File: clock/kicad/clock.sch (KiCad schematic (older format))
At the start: 82 parts, among them J1 USB-SS-52100-001, Q1 PN2222A, SW1 HOUR, SW2 MIN, SW3 TIME, U1 74HC4060, U10 74HC390, U11 NE555P, U12 74HC4511, U13 74HC4511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

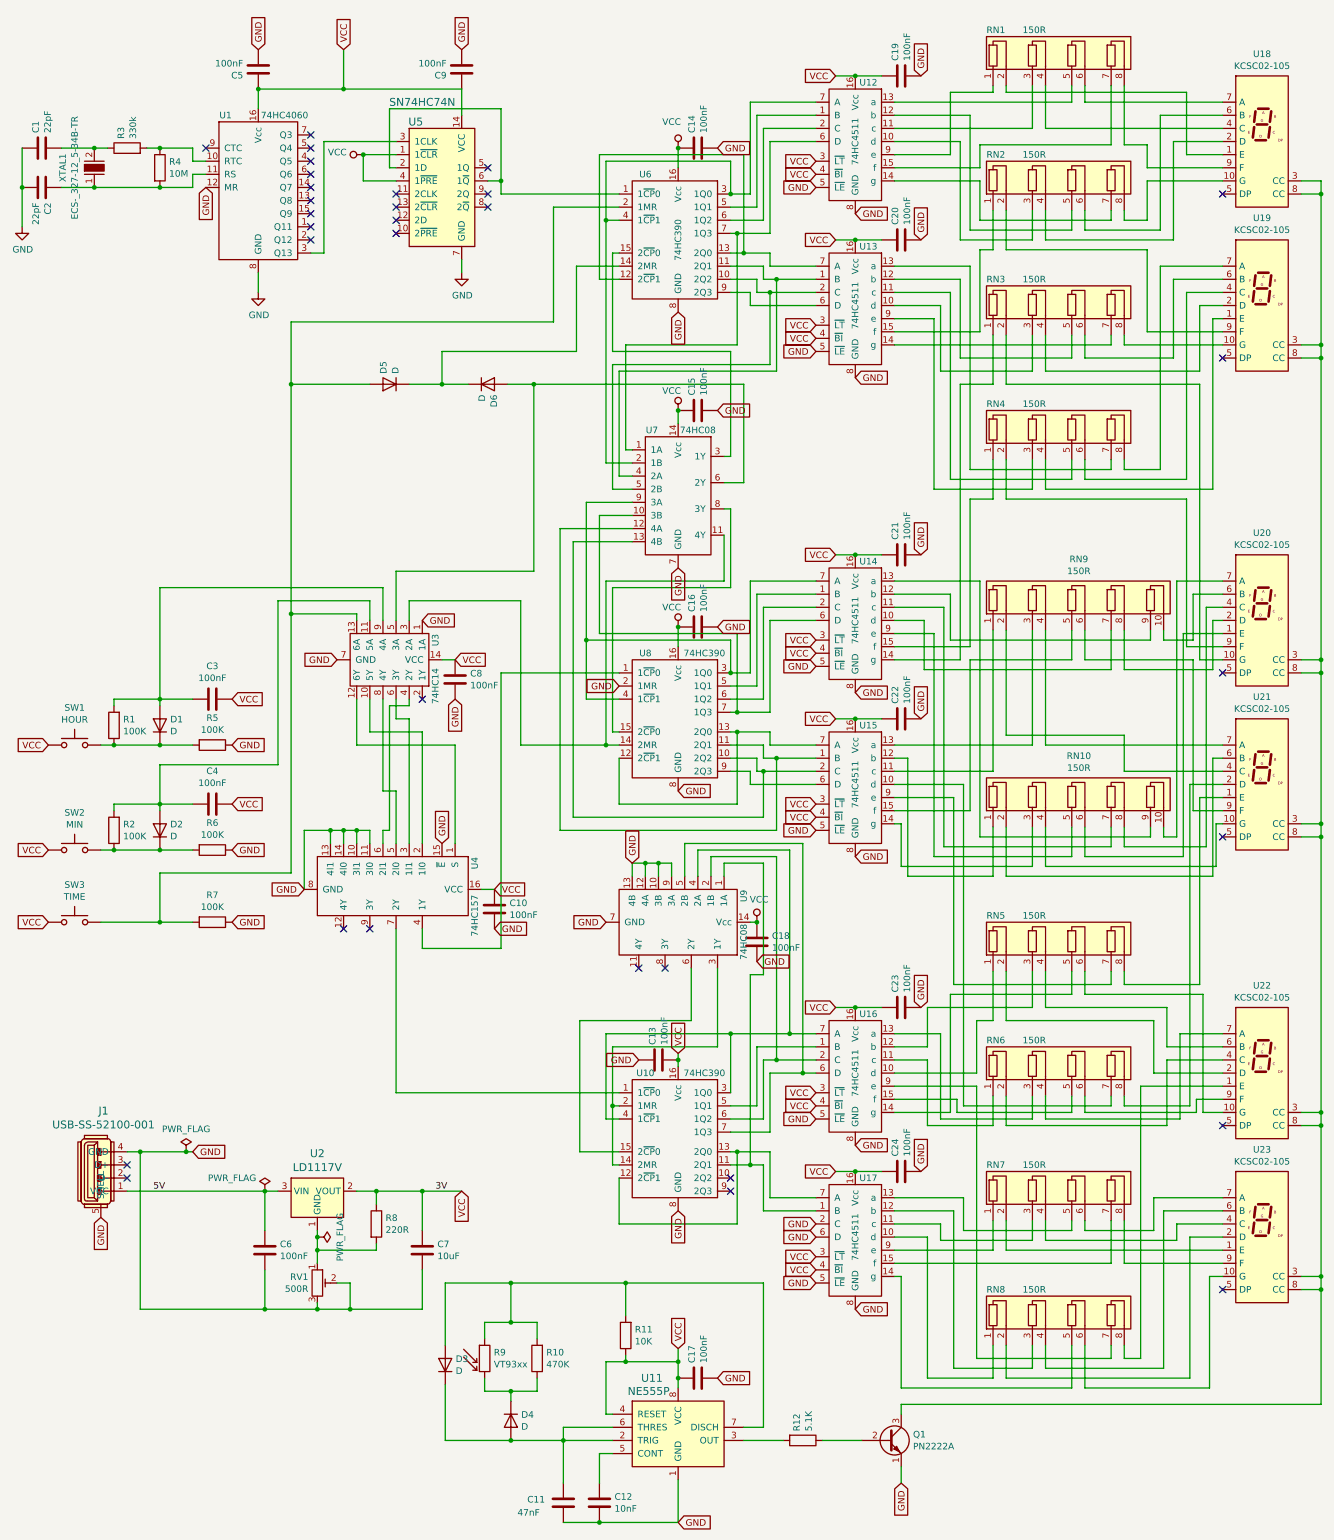
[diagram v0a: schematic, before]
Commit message: Clock: Switched 24H counter's high digit to quinary counter to match breadboard version.
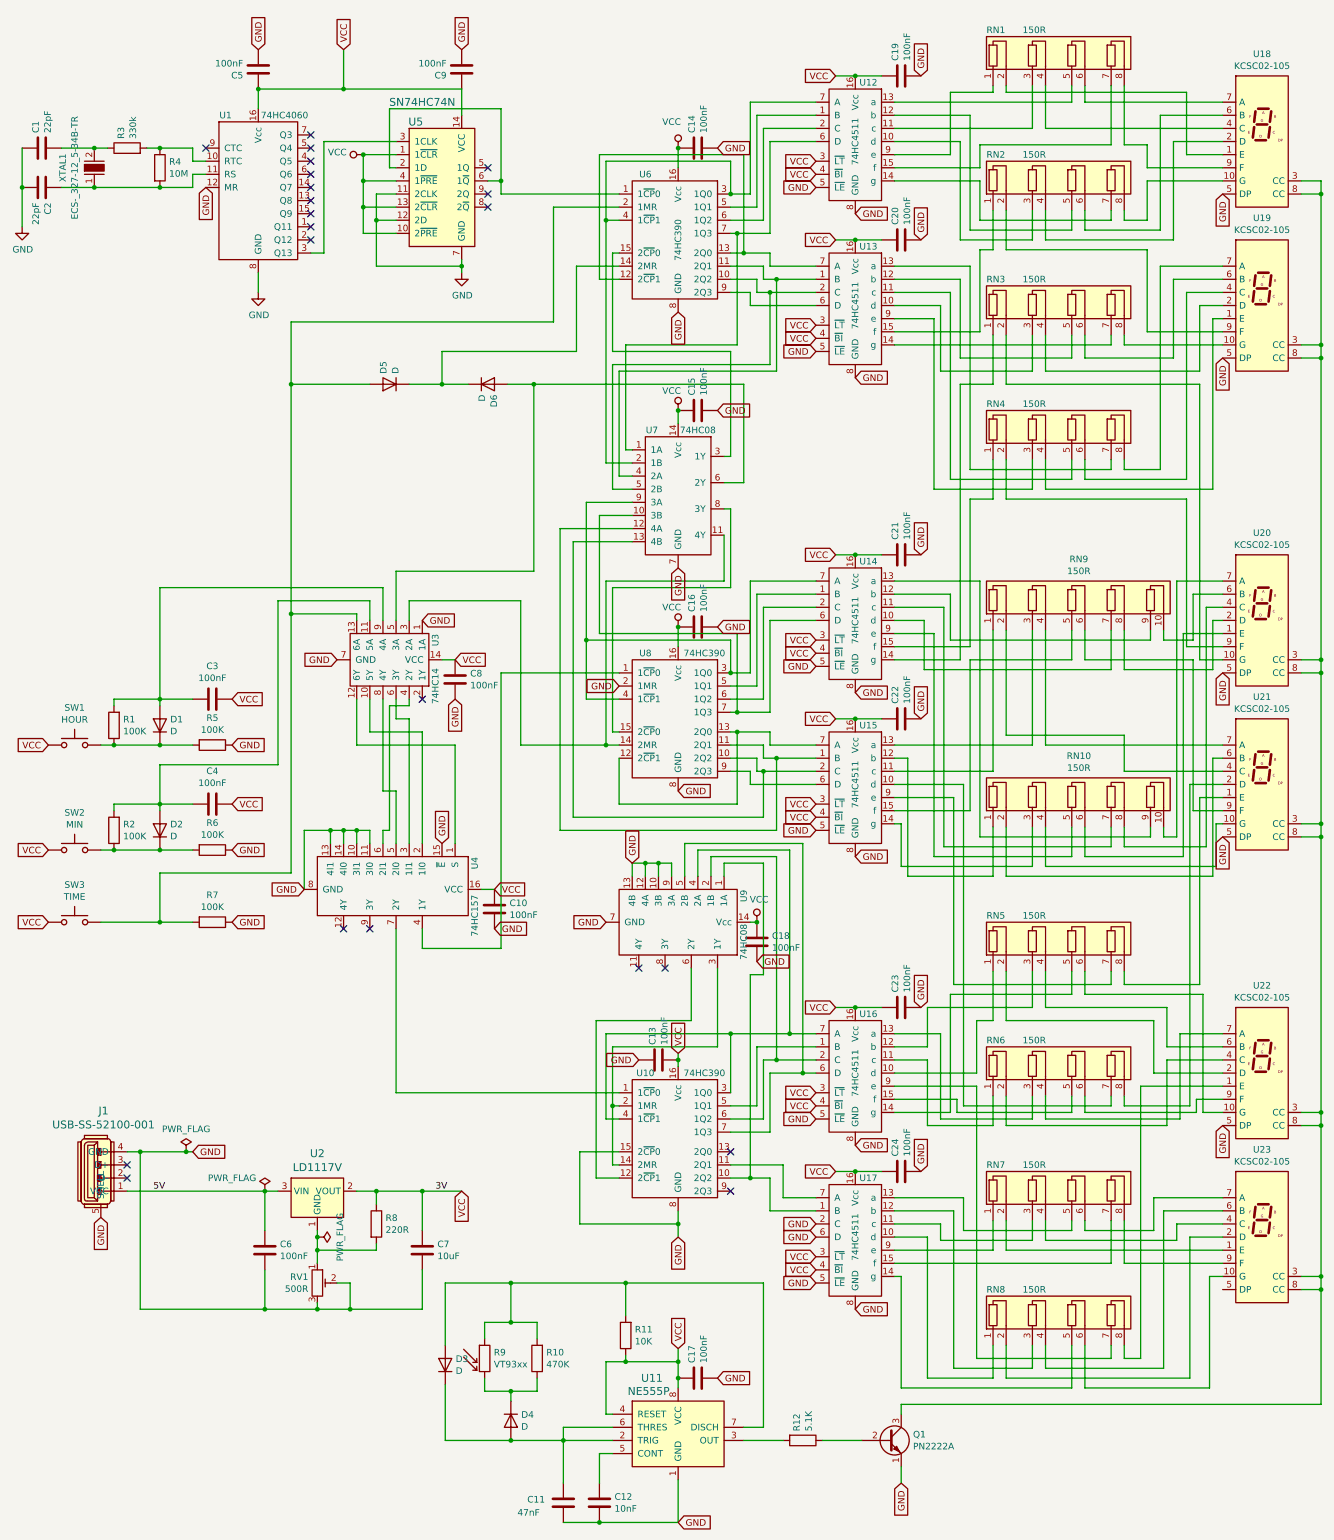
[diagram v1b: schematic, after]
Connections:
- net GND: now also U10.15 (2~CP~0), U18.5 (DP), U19.5 (DP), U20.5 (DP), U21.5 (DP), U22.5 (DP), U5.11 (2CLK), U5.12 (2D)
- net VCC: now also U5.10 (2~PRE), U5.13 (2~CLR)
- net at U17.1 (B), U9.1 (1A): now also U10.10 (2Q2); no longer U10.11 (2Q1)
- net at U9.6 (2Y): now also U10.12 (2~CP~1); no longer U10.15 (2~CP~0)
- new net: U10.11 (2Q1), U17.7 (A)
- now unconnected: U10.13 (2Q0)
- no-connect marks 32 -> 22
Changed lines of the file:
@@
 	2550 2450 2550 2600
 Wire Wire Line
-	4100 2350 4100 2450
+	4100 2350 4100 2400
 Wire Wire Line
 	3600 1650 3550 1650
@@
 	1    0    0    -1
 $EndComp
-NoConn ~ 3600 1850
-NoConn ~ 3600 1950
-NoConn ~ 3600 2050
-NoConn ~ 3600 2150
 NoConn ~ 2950 2200
 NoConn ~ 2950 2100
@@
 	1    0    0    -1
 $EndComp
-NoConn ~ 9900 1850
-NoConn ~ 9900 3100
 $Comp
 L clock:74HC390 U8
@@
 	1    0    0    -1
 $EndComp
-NoConn ~ 9900 5500
 Wire Wire Line
 	5150 5200 5150 4300
@@
 Wire Wire Line
 	6450 9000 6150 9000
-Wire Wire Line
-	6450 9150 6200 9150
-Wire Wire Line
-	6400 9250 6300 9250
-Text GLabel 5750 9600 3    50   Input ~ 0
+Text GLabel 5750 9800 3    50   Input ~ 0
 GND
 Text GLabel 5750 8400 1    50   Input ~ 0
@@
 	6700 6800 5800 6800
 Wire Wire Line
-	5800 6800 5800 7050
-Wire Wire Line
 	6350 8350 6800 8350
 Wire Wire Line
@@
 	5850 7750 5850 8150
 Wire Wire Line
-	5850 8150 5000 8150
-Wire Wire Line
-	5000 8150 5000 9150
-Wire Wire Line
-	5000 9150 5300 9150
-Wire Wire Line
-	6200 9150 6200 9700
-Wire Wire Line
-	6200 9700 5300 9700
-Wire Wire Line
-	5300 9700 5300 9350
-Connection ~ 6200 9150
-Wire Wire Line
-	6200 9150 6150 9150
-NoConn ~ 6150 9350
+	5850 8150 5125 8150
 NoConn ~ 6150 9450
 Text GLabel 6800 6600 0    50   Input ~ 0
@@
 Text GLabel 6800 6700 0    50   Input ~ 0
 GND
-NoConn ~ 9900 6750
 Text GLabel 7100 6900 2    50   Input ~ 0
 GND
@@
 	6150 8250 6600 8250
 Wire Wire Line
-	6300 9250 6300 7800
-Wire Wire Line
 	6300 7800 6400 7800
 Wire Wire Line
@@
 Wire Wire Line
 	6100 6950 6100 7050
-Connection ~ 6300 9250
-Wire Wire Line
-	6300 9250 6150 9250
 Text GLabel 2150 1800 3    50   Input ~ 0
 GND
@@
 Wire Wire Line
 	7450 11075 7450 11150
-Wire Wire Line
-	6400 9600 6400 9250
-Wire Wire Line
-	6450 9500 6450 9150
 Text GLabel 7600 9300 1    50   Input ~ 0
 GND
@@
 	1    0    0    -1
 $EndComp
-Wire Wire Line
-	6400 9600 6800 9600
-Wire Wire Line
-	6450 9500 6800 9500
-NoConn ~ 9900 10200
-NoConn ~ 9900 8950
 Connection ~ 10650 10200
 Connection ~ 10650 10100
@@
 	9150 2050 9325 2050
 Wire Wire Line
-	9325 2050 9325 1750
-Wire Wire Line
-	9325 1750 9900 1750
-Wire Wire Line
 	7400 2900 8050 2900
 Wire Wire Line
@@
 Wire Wire Line
 	2800 3300 2800 5050
+Wire Wire Line
+	3350 1750 3350 1950
+Wire Wire Line
+	3350 2150 3600 2150
+Connection ~ 3350 1750
+Wire Wire Line
+	3600 1950 3350 1950
+Connection ~ 3350 1950
+Wire Wire Line
+	3350 1950 3350 2150
+Wire Wire Line
+	3600 1850 3450 1850
+Wire Wire Line
+	3450 1850 3450 2050
+Wire Wire Line
+	3450 2400 4100 2400
+Connection ~ 4100 2400
+Wire Wire Line
+	4100 2400 4100 2450
+Wire Wire Line
+	3600 2050 3450 2050
+Connection ~ 3450 2050
+Wire Wire Line
+	3450 2050 3450 2400
+Text GLabel 9900 1850 3    50   Input ~ 0
+GND
+Text GLabel 9900 3100 3    50   Input ~ 0
+GND
+Text GLabel 9900 5500 3    50   Input ~ 0
+GND
+Text GLabel 9900 6750 3    50   Input ~ 0
+GND
+Text GLabel 9900 8950 3    50   Input ~ 0
+GND
+Wire Wire Line
+	9325 2050 9325 1750
+Wire Wire Line
+	9325 1750 9900 1750
+Wire Wire Line
+	5300 9150 5000 9150
+Wire Wire Line
+	5125 9350 5300 9350
+Wire Wire Line
+	5125 8150 5125 9350
+Wire Wire Line
+	5800 6800 5800 7050
+NoConn ~ 6150 9150
+Wire Wire Line
+	6150 9350 6300 9350
+Wire Wire Line
+	6450 9350 6450 9600
+Wire Wire Line
+	6450 9600 6800 9600
+Wire Wire Line
+	6550 9250 6550 9500
+Wire Wire Line
+	6550 9500 6800 9500
+Wire Wire Line
+	6150 9250 6550 9250
+Wire Wire Line
+	6300 7800 6300 9350
+Connection ~ 6300 9350
+Wire Wire Line
+	6300 9350 6450 9350
+Wire Wire Line
+	5000 9150 5000 9700
+Wire Wire Line
+	5000 9700 5750 9700
+Wire Wire Line
+	5750 9600 5750 9700
+Connection ~ 5750 9700
+Wire Wire Line
+	5750 9700 5750 9800
 $EndSCHEMATC

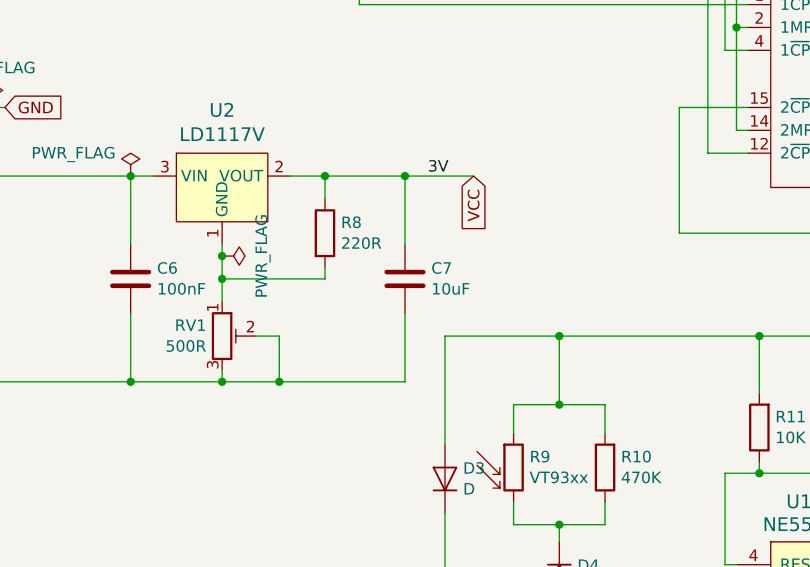
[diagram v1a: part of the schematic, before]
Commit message: Clock: Changed electrolytic capacitor's footprint to polarized one.
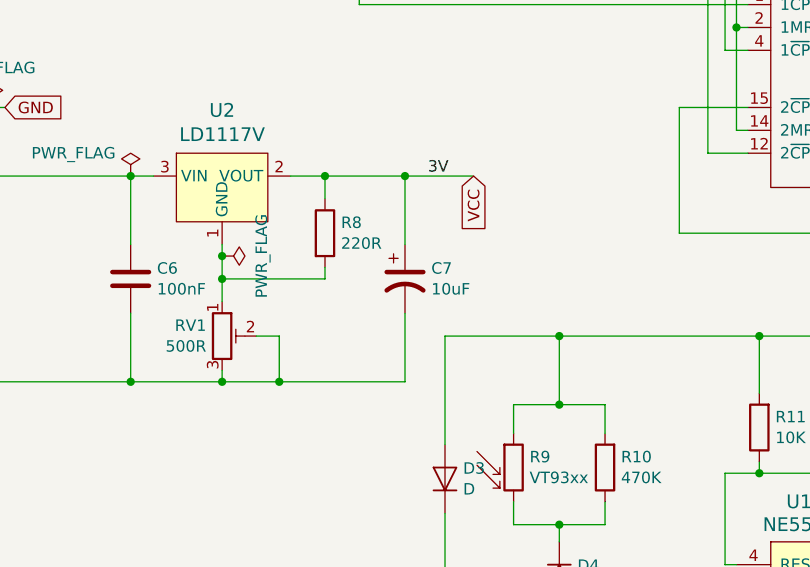
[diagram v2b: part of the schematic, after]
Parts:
- removed C7: 10uF, Capacitor_THT:C_Radial_D5.0mm_H11.0mm_P2.00mm, symbol Device:C
- added C7: 10uF, Capacitor_THT:CP_Radial_Tantal_D5.0mm_P2.50mm, symbol Device:CP1
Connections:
- net GND: now also C7.2
- net VCC: now also C7.1
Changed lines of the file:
@@
 	3450 9450 3450 9550
 Connection ~ 3450 9450
-$Comp
-L Device:C C7
-U 1 1 5DB38DC1
-P 3800 9900
-F 0 "C7" H 3915 9946 50  0000 L CNN
-F 1 "10uF" H 3915 9855 50  0000 L CNN
-F 2 "Capacitor_THT:C_Radial_D5.0mm_H11.0mm_P2.00mm" H 3838 9750 50  0001 C CNN
-F 3 "~" H 3800 9900 50  0001 C CNN
-	1    3800 9900
-	1    0    0    -1
-$EndComp
 Wire Wire Line
 	2600 9750 2600 9450
@@
 Wire Wire Line
 	5750 9700 5750 9800
+$Comp
+L Device:CP1 C7
+U 1 1 674B0372
+P 3800 9900
+F 0 "C7" H 3915 9946 50  0000 L CNN
+F 1 "10uF" H 3915 9855 50  0000 L CNN
+F 2 "Capacitor_THT:CP_Radial_Tantal_D5.0mm_P2.50mm" H 3800 9900 50  0001 C CNN
+F 3 "~" H 3800 9900 50  0001 C CNN
+	1    3800 9900
+	1    0    0    -1
+$EndComp
 $EndSCHEMATC
